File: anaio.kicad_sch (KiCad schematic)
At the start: 7 parts, among them J42 Conn_01x04, J43 Conn_01x02, J44 Conn_01x02, J45 Conn_01x02, J46 Conn_01x02, U23 TCA9535PWR(UMW)

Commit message: WIP v0.2.0 changes
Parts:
- removed J42: Conn_01x04, HL_Connector_Pad_2.54mm:Pad_1x04_P2.54_1.7x1.7_Rect-Oct, symbol Connector_Generic:Conn_01x04
- added J26, J31: Conn_01x04, HL_Connector_Pad_2.54mm:Pad_1x04_P2.54_1.7x1.7_Rect, symbol Connector_Generic:Conn_01x04
- renumbered J43 to J37, J44 to J38, J45 to J39, J46 to J40
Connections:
- net GND: now also J26.1 (Pin_1), J26.2 (Pin_2), J26.3 (Pin_3), J26.4 (Pin_4), J31.1 (Pin_1), J31.2 (Pin_2), J31.3 (Pin_3), J31.4 (Pin_4)
- net ~{INT}: no longer names the net of U23.1 (~{INT})
- no-connect marks 0 -> 1

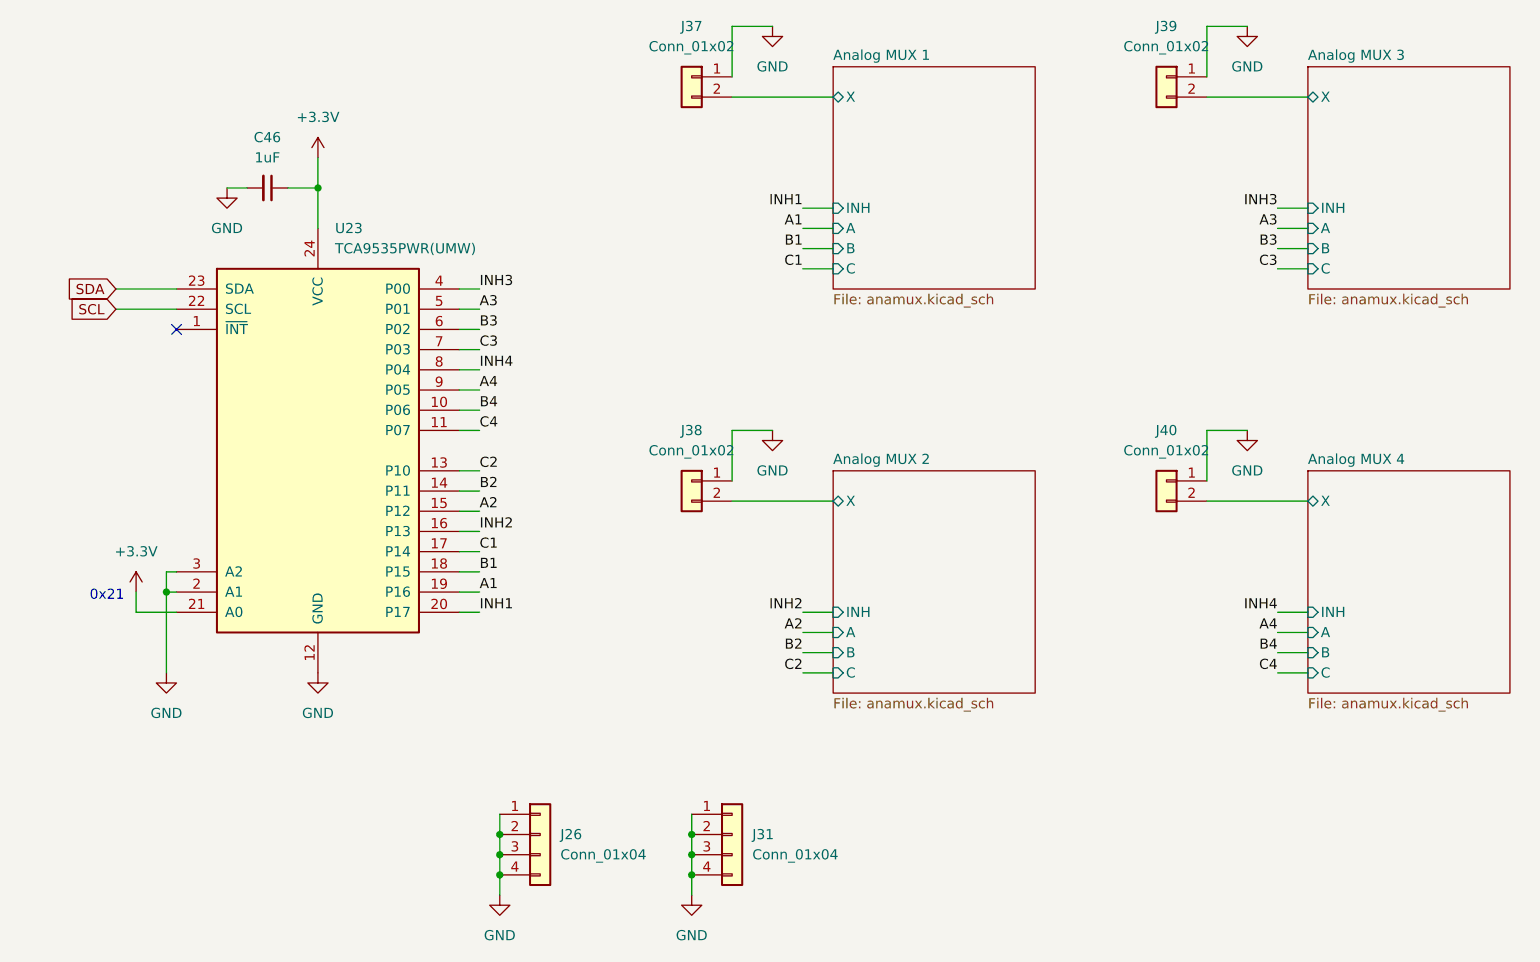
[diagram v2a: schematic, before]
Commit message: Assign part numbers and finish other 0.2.0 changes
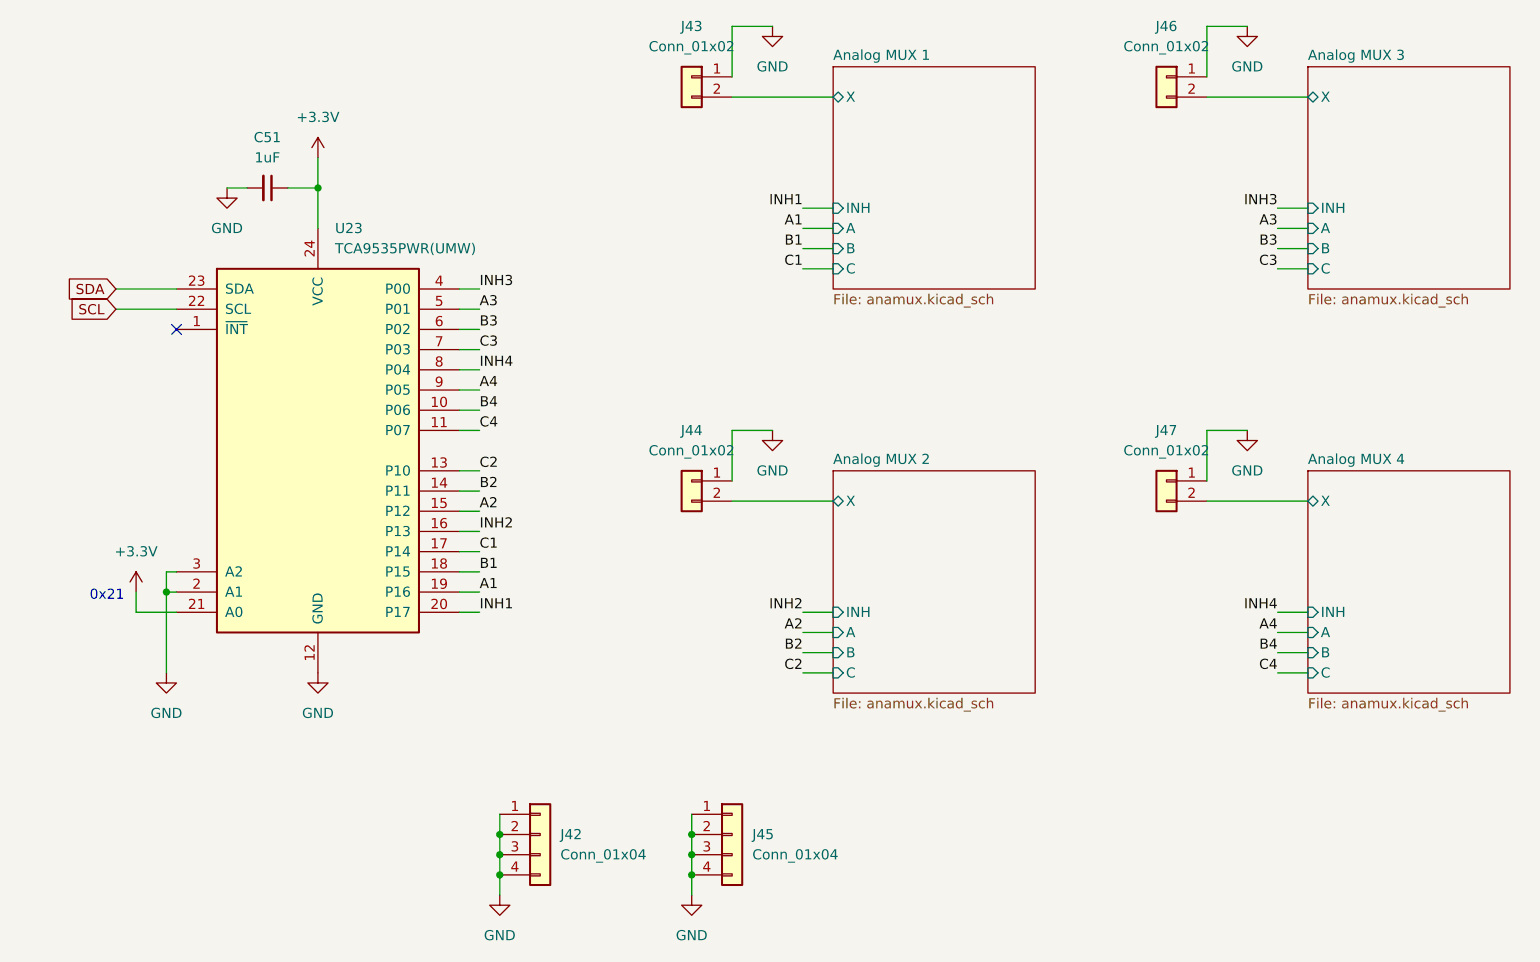
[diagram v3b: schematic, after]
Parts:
- J42: renamed from J26; LCSC (none) -> C2691448
- J43: renamed from J37; LCSC (none) -> C492401
- J44: renamed from J38; LCSC (none) -> C492401
- J45: renamed from J31; LCSC (none) -> C2691448
- J46: renamed from J39; LCSC (none) -> C492401
- J47: renamed from J40; LCSC (none) -> C492401
- renumbered C46 to C51
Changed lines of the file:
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@@
+		(polyline
+			(pts
+				(xy 55.88 85.725) (xy 55.88 77.47) (xy 53.34 77.47) (xy 53.34 85.725)
+			)
+			(stroke
+				(width 0)
+				(type dash)
+			)
+			(fill
+				(type none)
+			)
+		)
+	)
+	(rule_area
 		(polyline
 			(pts
 				(xy 93.98 121.92) (xy 93.98 78.74) (xy 91.44 78.74) (xy 91.44 121.92)
-			)
-			(stroke
-				(width 0)
-				(type dash)
-			)
-			(fill
-				(type none)
-			)
-		)
-	)
-	(rule_area
-		(polyline
-			(pts
-				(xy 55.88 85.725) (xy 55.88 77.47) (xy 53.34 77.47) (xy 53.34 85.725)
 			)
 			(stroke
@@
 		(dnp no)
 		(fields_autoplaced yes)
-		(property "Reference" "J38"
+		(property "Reference" "J44"
 			(at 121.92 97.79 0)
 			(effects
@@
 			)
 		)
+		(property "LCSC" "C492401"
+			(at 121.92 104.14 0)
+			(effects
+				(font
+					(size 1.27 1.27)
+				)
+				(hide yes)
+			)
+		)
 		(pin "2"
 		)
@@
 			(project "HALSPA"
 				(path "/7eeba806-440e-4671-bc07-69fe183910a7/c1640104-e93c-4dad-89ee-86b02155c684"
-					(reference "J38")
+					(reference "J44")
 					(unit 1)
 				)
@@
 		(dnp no)
 		(fields_autoplaced yes)
-		(property "Reference" "J26"
+		(property "Reference" "J42"
 			(at 105.41 148.5899 0)
 			(effects
@@
 			)
 		)
+		(property "LCSC" "C2691448"
+			(at 102.87 148.59 0)
+			(effects
+				(font
+					(size 1.27 1.27)
+				)
+				(hide yes)
+			)
+		)
 		(pin "4"
 		)
@@
 			(project ""
 				(path "/7eeba806-440e-4671-bc07-69fe183910a7/c1640104-e93c-4dad-89ee-86b02155c684"
-					(reference "J26")
+					(reference "J42")
 					(unit 1)
 				)
@@
 		(dnp no)
 		(fields_autoplaced yes)
-		(property "Reference" "#PWR0177"
+		(property "Reference" "#PWR0187"
 			(at 55.88 134.62 0)
 			(effects
@@
 			(project "HALSPA"
 				(path "/7eeba806-440e-4671-bc07-69fe183910a7/c1640104-e93c-4dad-89ee-86b02155c684"
-					(reference "#PWR0177")
+					(reference "#PWR0187")
 					(unit 1)
 				)
@@
 		(dnp no)
 		(fields_autoplaced yes)
-		(property "Reference" "#PWR0180"
+		(property "Reference" "#PWR0190"
 			(at 74.93 134.62 0)
 			(effects
@@
 			(project "HALSPA"
 				(path "/7eeba806-440e-4671-bc07-69fe183910a7/c1640104-e93c-4dad-89ee-86b02155c684"
-					(reference "#PWR0180")
+					(reference "#PWR0190")
 					(unit 1)
 				)
@@
 		(dnp no)
 		(fields_autoplaced yes)
-		(property "Reference" "#PWR0182"
+		(property "Reference" "#PWR0194"
 			(at 132.08 104.14 0)
 			(effects
@@
 			(project "HALSPA"
 				(path "/7eeba806-440e-4671-bc07-69fe183910a7/c1640104-e93c-4dad-89ee-86b02155c684"
-					(reference "#PWR0182")
+					(reference "#PWR0194")
 					(unit 1)
 				)
@@
 		(dnp no)
 		(fields_autoplaced yes)
-		(property "Reference" "J40"
+		(property "Reference" "J47"
 			(at 181.61 97.79 0)
 			(effects
@@
 			)
 		)
+		(property "LCSC" "C492401"
+			(at 181.61 104.14 0)
+			(effects
+				(font
+					(size 1.27 1.27)
+				)
+				(hide yes)
+			)
+		)
 		(pin "2"
 		)
@@
 			(project "HALSPA"
 				(path "/7eeba806-440e-4671-bc07-69fe183910a7/c1640104-e93c-4dad-89ee-86b02155c684"
-					(reference "J40")
+					(reference "J47")
 					(unit 1)
 				)
@@
 		(dnp no)
 		(fields_autoplaced yes)
-		(property "Reference" "J31"
+		(property "Reference" "J45"
 			(at 129.54 148.5899 0)
 			(effects
@@
 			)
 		)
+		(property "LCSC" "C2691448"
+			(at 127 148.59 0)
+			(effects
+				(font
+					(size 1.27 1.27)
+				)
+				(hide yes)
+			)
+		)
 		(pin "4"
 		)
@@
 			(project "HALSPA"
 				(path "/7eeba806-440e-4671-bc07-69fe183910a7/c1640104-e93c-4dad-89ee-86b02155c684"
-					(reference "J31")
+					(reference "J45")
 					(unit 1)
 				)
@@
 		(dnp no)
 		(fields_autoplaced yes)
-		(property "Reference" "#PWR0184"
+		(property "Reference" "#PWR0196"
 			(at 191.77 104.14 0)
 			(effects
@@
 			(project "HALSPA"
 				(path "/7eeba806-440e-4671-bc07-69fe183910a7/c1640104-e93c-4dad-89ee-86b02155c684"
-					(reference "#PWR0184")
+					(reference "#PWR0196")
 					(unit 1)
 				)
@@
 		(dnp no)
 		(fields_autoplaced yes)
-		(property "Reference" "#PWR0185"
+		(property "Reference" "#PWR0191"
 			(at 97.79 162.56 0)
 			(effects
@@
 			(project "HALSPA"
 				(path "/7eeba806-440e-4671-bc07-69fe183910a7/c1640104-e93c-4dad-89ee-86b02155c684"
-					(reference "#PWR0185")
+					(reference "#PWR0191")
 					(unit 1)
 				)
@@
 		(dnp no)
 		(fields_autoplaced yes)
-		(property "Reference" "#PWR0179"
+		(property "Reference" "#PWR0189"
 			(at 74.93 67.31 0)
 			(effects
@@
 			(project "HALSPA"
 				(path "/7eeba806-440e-4671-bc07-69fe183910a7/c1640104-e93c-4dad-89ee-86b02155c684"
-					(reference "#PWR0179")
+					(reference "#PWR0189")
 					(unit 1)
 				)
@@
 		(dnp no)
 		(fields_autoplaced yes)
-		(property "Reference" "#PWR0181"
+		(property "Reference" "#PWR0193"
 			(at 132.08 53.34 0)
 			(effects
@@
 			(project "HALSPA"
 				(path "/7eeba806-440e-4671-bc07-69fe183910a7/c1640104-e93c-4dad-89ee-86b02155c684"
-					(reference "#PWR0181")
+					(reference "#PWR0193")
 					(unit 1)
 				)
@@
 		(dnp no)
 		(fields_autoplaced yes)
-		(property "Reference" "#PWR0176"
+		(property "Reference" "#PWR0186"
 			(at 52.07 121.92 0)
 			(effects
@@
 			(project "HALSPA"
 				(path "/7eeba806-440e-4671-bc07-69fe183910a7/c1640104-e93c-4dad-89ee-86b02155c684"
-					(reference "#PWR0176")
+					(reference "#PWR0186")
 					(unit 1)
 				)
@@
 		(dnp no)
 		(fields_autoplaced yes)
-		(property "Reference" "C46"
+		(property "Reference" "C51"
 			(at 68.5736 60.96 90)
 			(effects
@@
 			(project "HALSPA"
 				(path "/7eeba806-440e-4671-bc07-69fe183910a7/c1640104-e93c-4dad-89ee-86b02155c684"
-					(reference "C46")
+					(reference "C51")
 					(unit 1)
 				)
@@
 		(dnp no)
 		(fields_autoplaced yes)
-		(property "Reference" "#PWR0178"
+		(property "Reference" "#PWR0188"
 			(at 63.5 73.66 0)
 			(effects
@@
 			(project "HALSPA"
 				(path "/7eeba806-440e-4671-bc07-69fe183910a7/c1640104-e93c-4dad-89ee-86b02155c684"
-					(reference "#PWR0178")
+					(reference "#PWR0188")
 					(unit 1)
 				)
@@
 		(dnp no)
 		(fields_autoplaced yes)
-		(property "Reference" "#PWR0199"
+		(property "Reference" "#PWR0192"
 			(at 121.92 162.56 0)
 			(effects
@@
 			(project "HALSPA"
 				(path "/7eeba806-440e-4671-bc07-69fe183910a7/c1640104-e93c-4dad-89ee-86b02155c684"
-					(reference "#PWR0199")
+					(reference "#PWR0192")
 					(unit 1)
 				)
@@
 		(dnp no)
 		(fields_autoplaced yes)
-		(property "Reference" "#PWR0183"
+		(property "Reference" "#PWR0195"
 			(at 191.77 53.34 0)
 			(effects
@@
 			(project "HALSPA"
 				(path "/7eeba806-440e-4671-bc07-69fe183910a7/c1640104-e93c-4dad-89ee-86b02155c684"
-					(reference "#PWR0183")
+					(reference "#PWR0195")
 					(unit 1)
 				)
@@
 		(dnp no)
 		(fields_autoplaced yes)
-		(property "Reference" "J37"
+		(property "Reference" "J43"
 			(at 121.92 46.99 0)
 			(effects
@@
 			)
 		)
+		(property "LCSC" "C492401"
+			(at 121.92 53.34 0)
+			(effects
+				(font
+					(size 1.27 1.27)
+				)
+				(hide yes)
+			)
+		)
 		(pin "2"
 		)
@@
 			(project "HALSPA"
 				(path "/7eeba806-440e-4671-bc07-69fe183910a7/c1640104-e93c-4dad-89ee-86b02155c684"
-					(reference "J37")
+					(reference "J43")
 					(unit 1)
 				)
@@
 		(dnp no)
 		(fields_autoplaced yes)
-		(property "Reference" "J39"
+		(property "Reference" "J46"
 			(at 181.61 46.99 0)
 			(effects
@@
 			)
 		)
+		(property "LCSC" "C492401"
+			(at 181.61 53.34 0)
+			(effects
+				(font
+					(size 1.27 1.27)
+				)
+				(hide yes)
+			)
+		)
 		(pin "2"
 		)
@@
 			(project "HALSPA"
 				(path "/7eeba806-440e-4671-bc07-69fe183910a7/c1640104-e93c-4dad-89ee-86b02155c684"
-					(reference "J39")
-					(unit 1)
-				)
+					(reference "J46")
+					(unit 1)
+				)

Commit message: Update the title blocks
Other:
- company: (none) -> Hat Labs Oy
- title: (none) -> HALSPA - Hat Labs Spaghetti Board
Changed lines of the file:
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@@
 	(generator_version "9.0")
 	(paper "A4")
+	(title_block
+		(title "HALSPA - Hat Labs Spaghetti Board")
+		(date "2025-04-17")
+		(rev "v0.2.0")
+		(company "Hat Labs Oy")
+		(comment 1 "See the accompanying LICENSE.md file for license details.")
+	)
 	(text "0x21"
 		(exclude_from_sim no)

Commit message: Fix minor production issues
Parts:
- J42, J45: JLCPCB_CORRECTION (none) -> 0;3.81;270
- J43, J44, J46, J47: JLCPCB_CORRECTION (none) -> 0;1.27;270
- U23: LCSC C22396388 -> C130204
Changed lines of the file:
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@@
+			)
+		)
+		(property "JLCPCB_CORRECTION" "0;1.27;270"
+			(at 121.92 104.14 0)
+			(effects
+				(font
+					(size 1.27 1.27)
+				)
+				(hide yes)
 			)
 		)
@@
 		)
 		(property "LCSC" "C2691448"
+			(at 102.87 148.59 0)
+			(effects
+				(font
+					(size 1.27 1.27)
+				)
+				(hide yes)
+			)
+		)
+		(property "JLCPCB_CORRECTION" "0;3.81;270"
 			(at 102.87 148.59 0)
 			(effects
@@
 			)
 		)
+		(property "JLCPCB_CORRECTION" "0;1.27;270"
+			(at 181.61 104.14 0)
+			(effects
+				(font
+					(size 1.27 1.27)
+				)
+				(hide yes)
+			)
+		)
 		(pin "2"
 		)
@@
 			)
 		)
+		(property "JLCPCB_CORRECTION" "0;3.81;270"
+			(at 127 148.59 0)
+			(effects
+				(font
+					(size 1.27 1.27)
+				)
+				(hide yes)
+			)
+		)
 		(pin "4"
 		)
@@
 			)
 		)
-		(property "Datasheet" "https://www.lcsc.com/datasheet/lcsc_datasheet_2410010333_UMW-Youtai-Semiconductor-Co---Ltd--TCA9535PWR-UMW_C22396388.pdf"
+		(property "Datasheet" "https://www.ti.com/lit/ds/symlink/tca9535.pdf"
 			(at 62.23 77.47 0)
 			(effects
@@
 			)
 		)
-		(property "LCSC" "C22396388"
+		(property "LCSC" "C130204"
 			(at 74.93 100.33 0)
 			(effects
@@
 			)
 		)
+		(property "JLCPCB_CORRECTION" "0;1.27;270"
+			(at 121.92 53.34 0)
+			(effects
+				(font
+					(size 1.27 1.27)
+				)
+				(hide yes)
+			)
+		)
 		(pin "2"
 		)
@@
 			(at 181.61 53.34 0)
 			(effects
+				(font
+					(size 1.27 1.27)
+				)
+				(hide yes)
+			)
+		)
+		(property "JLCPCB_CORRECTION" "0;1.27;270"
+			(at 181.61 53.34 0)
+			(effects
